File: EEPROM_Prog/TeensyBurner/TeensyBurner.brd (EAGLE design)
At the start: 100 x 80 mm, 10 parts, among them IC1 74LS595N, IC2 74LS595N, J1 POWER_JACK

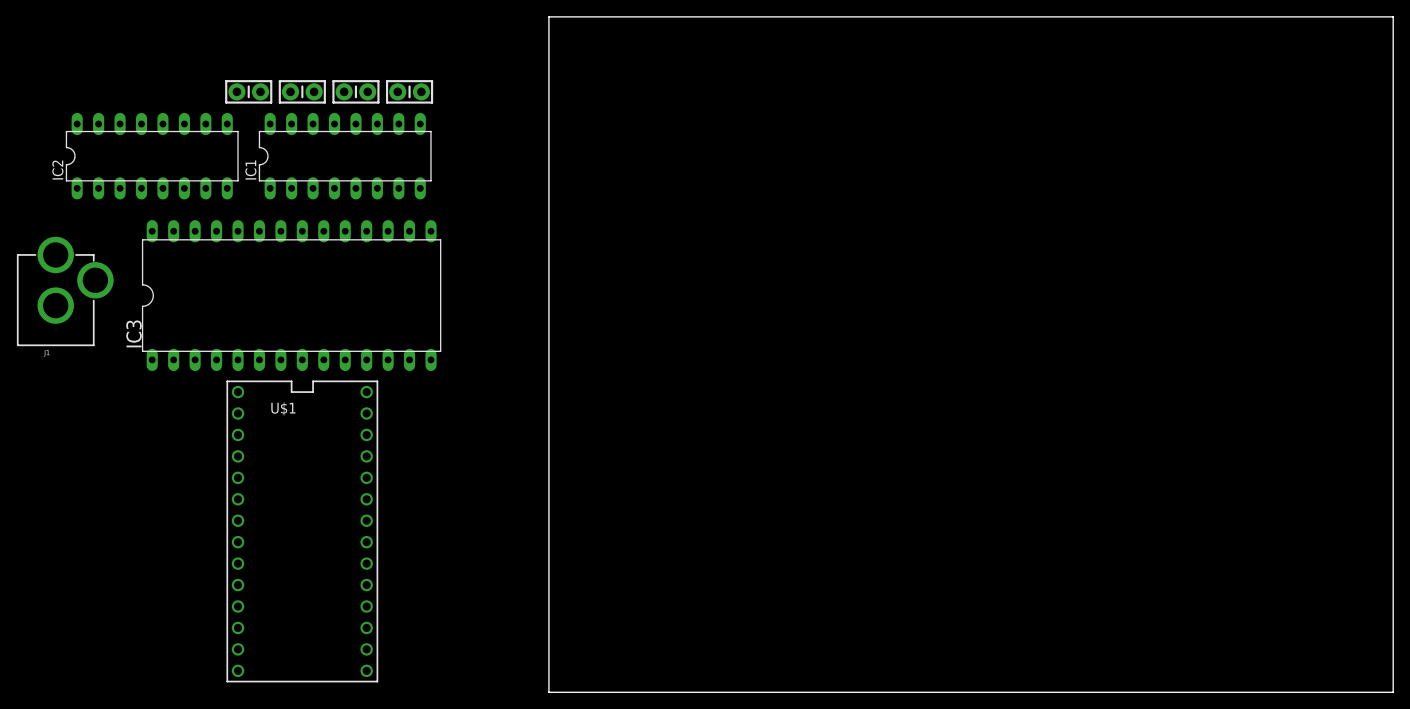
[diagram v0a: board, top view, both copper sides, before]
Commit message: Updated Eagle files
Upladed an old version, this corrected that.
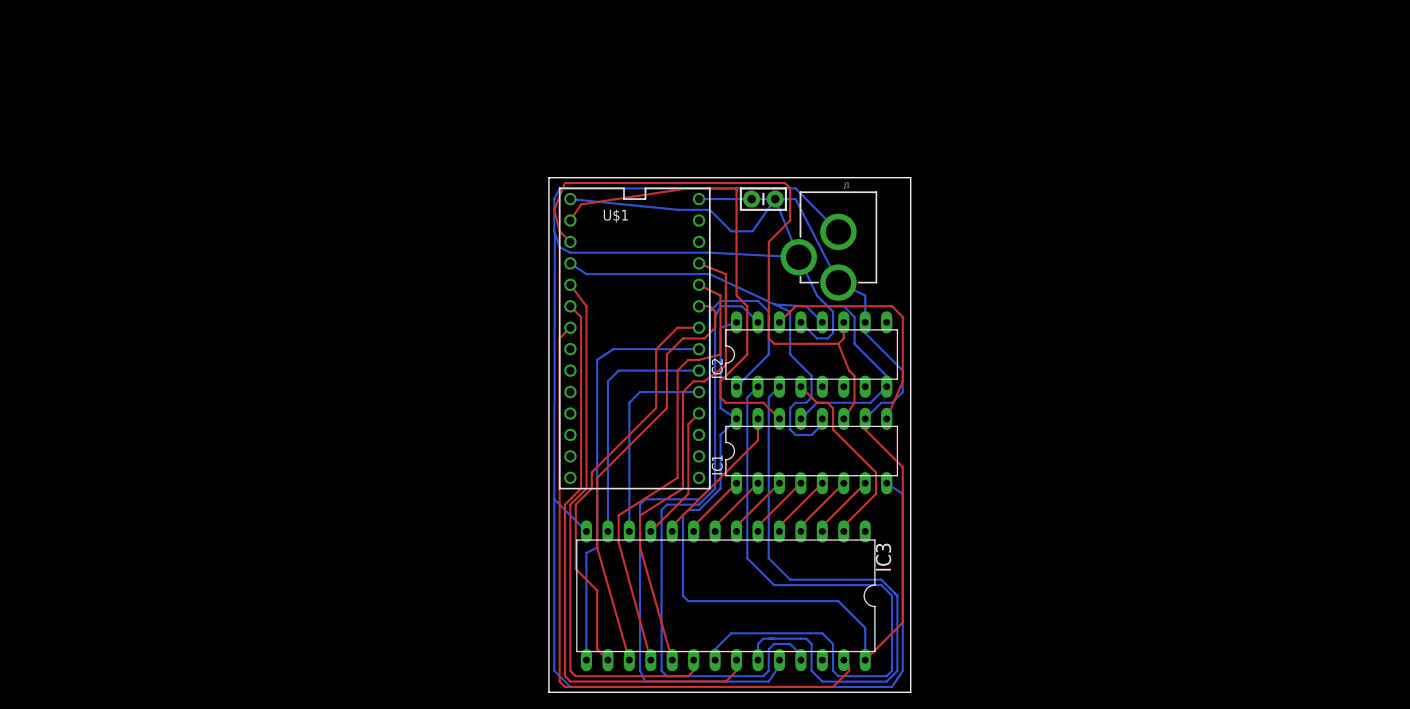
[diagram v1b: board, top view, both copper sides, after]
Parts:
- removed C1, C2, C3: 0.1uF, SparkFun-Capacitors:CAP-PTH-SMALL-KIT
- moved J1 95.8 mm to (34.3, 62.2), turned to 180 degrees
- moved IC2 81.6 mm to (31.1, 40.0)
- moved IC1 65.4 mm to (31.1, 28.6)
- moved IC3 62.5 mm to (21.0, 11.4), turned to 180 degrees
- moved C4 62.3 mm to (25.4, 58.4)
- moved U$1 45.5 mm to (10.2, 41.9)
- moved FRAME1 1.27 mm to (-40.6, 71.1)
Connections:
- removed net N$25: IC3.19, U$1.14/A0
- new net N$36: IC3.19, U$1.23/A9
- net GND: no longer C1.2, C2.2, C3.2
- net N$18: now also U$1.16/A2; no longer U$1.21/A7
- net N$19: now also U$1.17/A3; no longer U$1.20/A6
- net N$20: now also U$1.18/A4; no longer U$1.19/A5
- net N$21: now also U$1.19/A5; no longer U$1.18/A4
- net N$22: now also U$1.20/A6; no longer U$1.17/A3
- net N$23: now also U$1.21/A7; no longer U$1.16/A2
- net N$24: now also U$1.22/A8; no longer U$1.15/A1
- net VCC: no longer C1.1, C2.1, C3.1
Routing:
- net GND: track 0.00 -> 270.3 mm
- net VCC: track 0.00 -> 142.5 mm
- net N$14: track 0.00 -> 87.1 mm
- net N$32: track 0.00 -> 79.3 mm
- net N$15: track 0.00 -> 76.0 mm
- net N$4: track 0.00 -> 74.7 mm
- net N$13: track 0.00 -> 74.4 mm
- net N$16: track 0.00 -> 71.1 mm
- net N$31: track 0.00 -> 67.5 mm
- net N$30: track 0.00 -> 63.5 mm
- net N$3: track 0.00 -> 55.9 mm
- net N$36: track 0.00 -> 55.6 mm
- net N$2: track 0.00 -> 55.5 mm
- net N$24: track 0.00 -> 54.1 mm
- net N$23: track 0.00 -> 51.3 mm
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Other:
- board size 100 x 80 mm -> 42.9 x 61 mm
